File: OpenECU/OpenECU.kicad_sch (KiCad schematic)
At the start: 0 parts

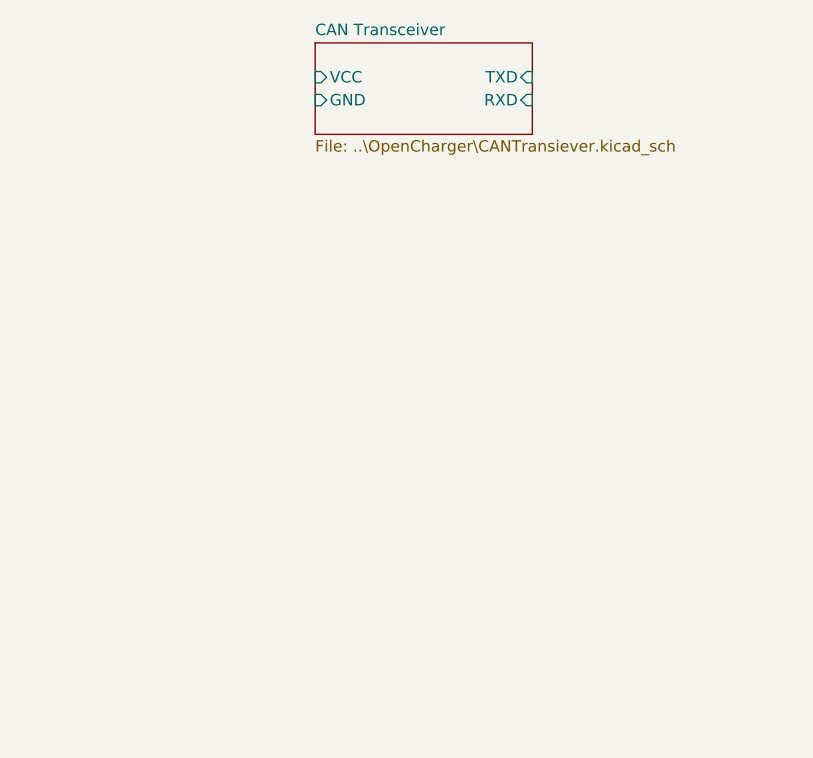
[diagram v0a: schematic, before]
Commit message: Updated Charger and MC
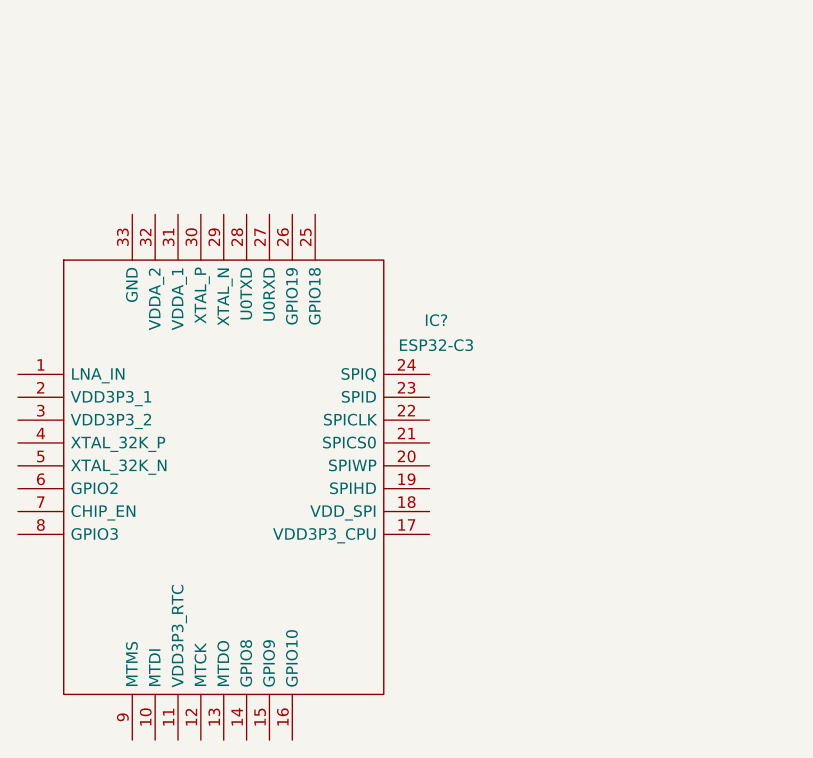
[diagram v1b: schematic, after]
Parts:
- added IC?: ESP32-C3, QFN50P500X500X90-33N-D, symbol SamacSys_Parts:ESP32-C3
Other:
- removed sheet CAN Transceiver
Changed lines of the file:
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@@
-(kicad_sch (version 20210621) (generator eeschema)
+(kicad_sch (version 20211123) (generator eeschema)
   (paper "A4")
-  (sheet (at 143.51 45.72) (size 24.13 10.16) (fields_autoplaced)
-    (stroke (width 0.1524) (type solid) (color 0 0 0 0))
-    (fill (color 0 0 0 0.0000))
-    (property "Sheet name" "CAN Transceiver" (id 0) (at 143.51 45.0084 0)
-      (effects (font (size 1.27 1.27)) (justify left bottom))
+  (symbol (lib_id "SamacSys_Parts:ESP32-C3") (at 110.49 82.55 0) (unit 1)
+    (in_bom yes) (on_board yes) (fields_autoplaced)
+    (property "Reference" "IC?" (id 0) (at 156.9703 76.5767 0))
+    (property "Value" "ESP32-C3" (id 1) (at 156.9703 79.3518 0))
+    (property "Footprint" "QFN50P500X500X90-33N-D" (id 2) (at 152.4 69.85 0)
+      (effects (font (size 1.27 1.27)) (justify left) hide)
     )
-    (property "Sheet file" "..\\OpenCharger\\CANTransiever.kicad_sch" (id 1) (at 143.51 56.4646 0)
-      (effects (font (size 1.27 1.27)) (justify left top))
+    (property "Datasheet" "https://www.espressif.com/sites/default/files/documentation/esp32-c3_datasheet_en.pdf" (id 3) (at 152.4 72.39 0)
+      (effects (font (size 1.27 1.27)) (justify left) hide)
     )
-    (pin "GND" input (at 143.51 52.07 180)
-      (effects (font (size 1.27 1.27)) (justify left))
+    (property "Description" "Ultra-Low-Power SoC with RISC-V Single-Core CPU" (id 4) (at 152.4 74.93 0)
+      (effects (font (size 1.27 1.27)) (justify left) hide)
     )
-    (pin "VCC" input (at 143.51 49.53 180)
-      (effects (font (size 1.27 1.27)) (justify left))
+    (property "Height" "0.9" (id 5) (at 152.4 77.47 0)
+      (effects (font (size 1.27 1.27)) (justify left) hide)
     )
-    (pin "TXD" input (at 167.64 49.53 0)
-      (effects (font (size 1.27 1.27)) (justify right))
+    (property "Mouser Part Number" "356-ESP32-C3" (id 6) (at 152.4 80.01 0)
+      (effects (font (size 1.27 1.27)) (justify left) hide)
     )
-    (pin "RXD" input (at 167.64 52.07 0)
-      (effects (font (size 1.27 1.27)) (justify right))
+    (property "Mouser Price/Stock" "https://www.mouser.co.uk/ProductDetail/Espressif-Systems/ESP32-C3?qs=iLbezkQI%252BsiMXe7tMG%252Bo%2FA%3D%3D" (id 7) (at 152.4 82.55 0)
+      (effects (font (size 1.27 1.27)) (justify left) hide)
     )
+    (property "Manufacturer_Name" "Espressif Systems" (id 8) (at 152.4 85.09 0)
+      (effects (font (size 1.27 1.27)) (justify left) hide)
+    )
+    (property "Manufacturer_Part_Number" "ESP32-C3" (id 9) (at 152.4 87.63 0)
+      (effects (font (size 1.27 1.27)) (justify left) hide)
+    )
+    (pin "1")
+    (pin "10")
+    (pin "11")
+    (pin "12")
+    (pin "13")
+    (pin "14")
+    (pin "15")
+    (pin "16")
+    (pin "17")
+    (pin "18")
+    (pin "19")
+    (pin "2")
+    (pin "20")
+    (pin "21")
+    (pin "22")
+    (pin "23")
+    (pin "24")
+    (pin "25")
+    (pin "26")
+    (pin "27")
+    (pin "28")
+    (pin "29")
+    (pin "3")
+    (pin "30")
+    (pin "31")
+    (pin "32")
+    (pin "33")
+    (pin "4")
+    (pin "5")
+    (pin "6")
+    (pin "7")
+    (pin "8")
+    (pin "9")
   )
   (sheet_instances
     (path "/" (page "1"))
-    (path "/24c94f61-8ecd-4025-a429-bda0d11e8681" (page "2"))
   )
   (symbol_instances
-    (path "/24c94f61-8ecd-4025-a429-bda0d11e8681/b6df074c-0d9b-4622-9934-6578c8579d2d"
-      (reference "C7") (unit 1) (value "C") (footprint "")
-    )
-    (path "/24c94f61-8ecd-4025-a429-bda0d11e8681/d881669f-f1ae-4865-a9bc-90fd749c7ac2"
-      (reference "J4") (unit 1) (value "RJ45_LED") (footprint "Connector_RJ:RJ45_Amphenol_RJHSE538X")
-    )
-    (path "/24c94f61-8ecd-4025-a429-bda0d11e8681/3222b3a7-6040-4e7e-8a22-06d0f1f57466"
-      (reference "R5") (unit 1) (value "R_US") (footprint "")
-    )
-    (path "/24c94f61-8ecd-4025-a429-bda0d11e8681/0efbffc9-e772-4b3d-b281-ecd1ead99e22"
-      (reference "R6") (unit 1) (value "R_US") (footprint "")
-    )
-    (path "/24c94f61-8ecd-4025-a429-bda0d11e8681/bdd6668c-03c1-43bd-84bc-e37c565b337b"
-      (reference "U1") (unit 1) (value "ISO1050DUB") (footprint "Package_SO:SOP-8_6.62x9.15mm_P2.54mm")
+    (path "/14c24f6d-c2bf-4b01-9d4b-7f0755e08445"
+      (reference "IC?") (unit 1) (value "ESP32-C3") (footprint "QFN50P500X500X90-33N-D")
     )
   )
